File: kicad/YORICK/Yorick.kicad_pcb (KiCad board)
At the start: 2 copper layers, 124 x 112 mm, 64 parts, among them J1 Conn_01x12, J2 AVR-ISP-6, J3 AudioJack2_SwitchT, J4 USB_B_Micro, J5 AudioJack2_SwitchT, Q1 Q_NJFET_DSG, Q2 Q_NJFET_DSG, SW1 SW_Push, SW2 SW_Push, U1 4069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

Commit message: Changing value for opamp pulldown resistor
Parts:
- R22: value 100k -> 1m
- R37: value 39k -> 33k
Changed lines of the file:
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@@
         (effects (font (size 1 1) (thickness 0.15)))
     )
-    (fp_text value "39k" (at 6.858 0.508) (layer "F.Fab")
+    (fp_text value "33k" (at 6.858 0.508) (layer "F.Fab")
         (effects (font (size 1 1) (thickness 0.15)))
     )
@@
         (effects (font (size 1 1) (thickness 0.15)))
     )
-    (fp_text value "100k" (at 6.35 0.508 90) (layer "F.Fab")
-        (effects (font (size 1 1) (thickness 0.15)))
-    )
+    (fp_text value "1m" (at 6.35 0.508 90) (layer "F.Fab")
+        (effects (font (size 1 1) (thickness 0.15)))
+    )

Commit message: Tweaking values for some parts
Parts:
- R16, R25: value 47r -> 18r
- R20, R21: value 2k2 -> rled
- RV1, RV2, RV3: value 100k -> 100kB
- RV4: value 10k -> 10kB
- RV5: value 100k -> 100kA
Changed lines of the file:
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@@
     (descr "https://www.omron.com/ecb/products/pdf/en-b3f.pdf")
     (tags "tact sw push 6mm")
+    (property "Part" "Omron B3F-1070 Extended")
     (property "Sheetfile" "Yorick.kicad_sch")
     (property "Sheetname" "")
@@
         (effects (font (size 1 1) (thickness 0.15)))
     )
-    (fp_text value "47r" (at 6.858 0.508 90) (layer "F.Fab")
+    (fp_text value "18r" (at 6.858 0.508 90) (layer "F.Fab")
         (effects (font (size 1 1) (thickness 0.15)))
     )
@@
         (effects (font (size 1 1) (thickness 0.15)))
     )
-    (fp_text value "47r" (at 3.302 -0.508 90) (layer "F.Fab")
+    (fp_text value "18r" (at 3.302 -0.508 90) (layer "F.Fab")
         (effects (font (size 1 1) (thickness 0.15)))
     )
@@
         (effects (font (size 1 1) (thickness 0.15)))
     )
-    (fp_text value "2k2" (at 3.302 -0.508 90) (layer "F.Fab")
+    (fp_text value "rled" (at 3.302 -0.508 90) (layer "F.Fab")
         (effects (font (size 1 1) (thickness 0.15)))
     )
@@
         (effects (font (size 1 1) (thickness 0.15)))
     )
-    (fp_text value "100k" (at 2.032 -0.04 -180) (layer "F.Fab")
+    (fp_text value "100kB" (at 2.032 -0.04 -180) (layer "F.Fab")
         (effects (font (size 1 1) (thickness 0.15)))
     )
@@
         (effects (font (size 1 1) (thickness 0.15)))
     )
-    (fp_text value "100k" (at 1.778 -0.04 -180) (layer "F.Fab")
+    (fp_text value "100kB" (at 1.778 -0.04 -180) (layer "F.Fab")
         (effects (font (size 1 1) (thickness 0.15)))
     )
@@
         (effects (font (size 1 1) (thickness 0.15)))
     )
-    (fp_text value "10k" (at 1.912 -0.014) (layer "F.Fab")
+    (fp_text value "10kB" (at 1.912 -0.014) (layer "F.Fab")
         (effects (font (size 1 1) (thickness 0.15)))
     )
@@
         (effects (font (size 1 1) (thickness 0.15)))
     )
-    (fp_text value "100k" (at 2.166 -0.014) (layer "F.Fab")
+    (fp_text value "100kA" (at 2.166 -0.014) (layer "F.Fab")
         (effects (font (size 1 1) (thickness 0.15)))
     )
@@
         (effects (font (size 1 1) (thickness 0.15)))
     )
-    (fp_text value "2k2" (at 3.302 -0.508 90) (layer "F.Fab")
+    (fp_text value "rled" (at 3.302 -0.508 90) (layer "F.Fab")
         (effects (font (size 1 1) (thickness 0.15)))
     )
@@
         (effects (font (size 1 1) (thickness 0.15)))
     )
-    (fp_text value "100k" (at 1.912 -0.028) (layer "F.Fab")
+    (fp_text value "100kB" (at 1.912 -0.028) (layer "F.Fab")
         (effects (font (size 1 1) (thickness 0.15)))
     )

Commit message: Updating parts and build info
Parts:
- R20, R21: value rled -> 1k
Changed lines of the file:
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@@
         (effects (font (size 1 1) (thickness 0.15)))
     )
-    (fp_text value "rled" (at 3.302 -0.508 90) (layer "F.Fab")
+    (fp_text value "1k" (at 3.302 -0.508 90) (layer "F.Fab")
         (effects (font (size 1 1) (thickness 0.15)))
     )
@@
         (effects (font (size 1 1) (thickness 0.15)))
     )
-    (fp_text value "rled" (at 3.302 -0.508 90) (layer "F.Fab")
+    (fp_text value "1k" (at 3.302 -0.508 90) (layer "F.Fab")
         (effects (font (size 1 1) (thickness 0.15)))
     )

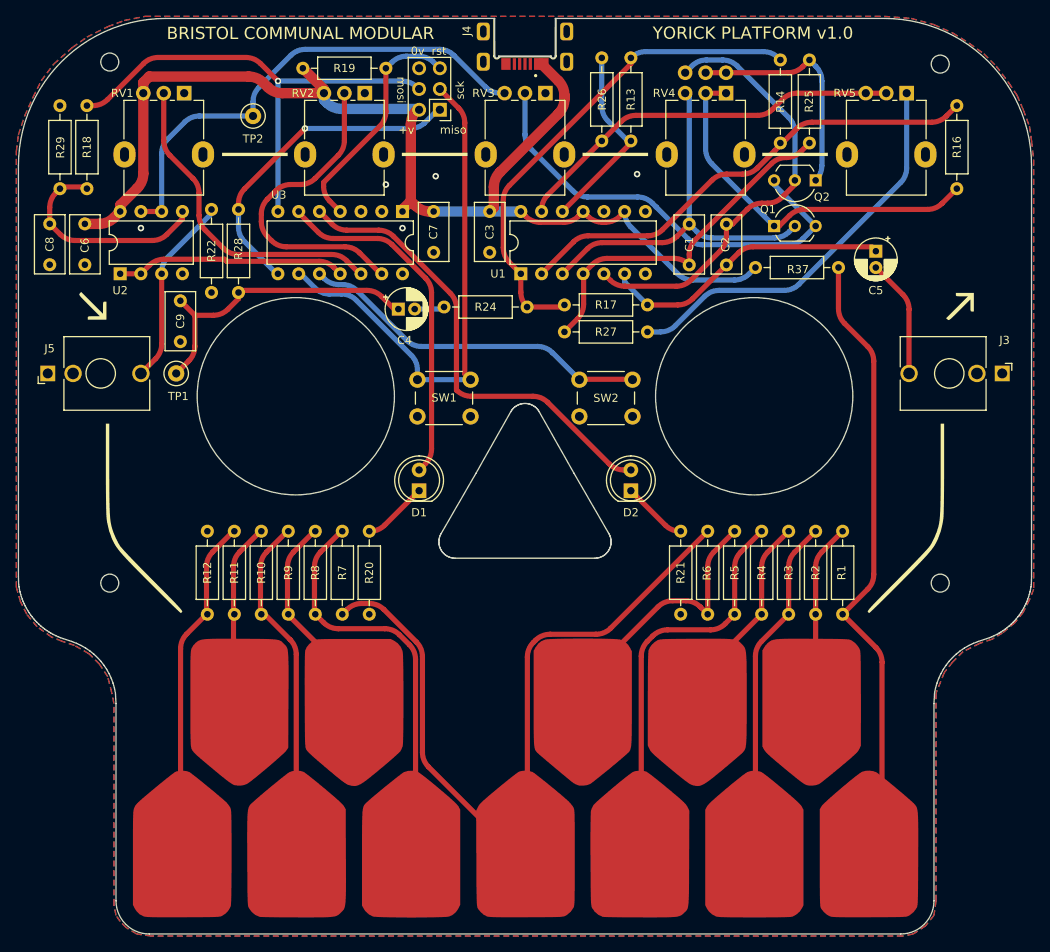
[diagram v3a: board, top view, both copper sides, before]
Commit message: Adding capacitors after some testing
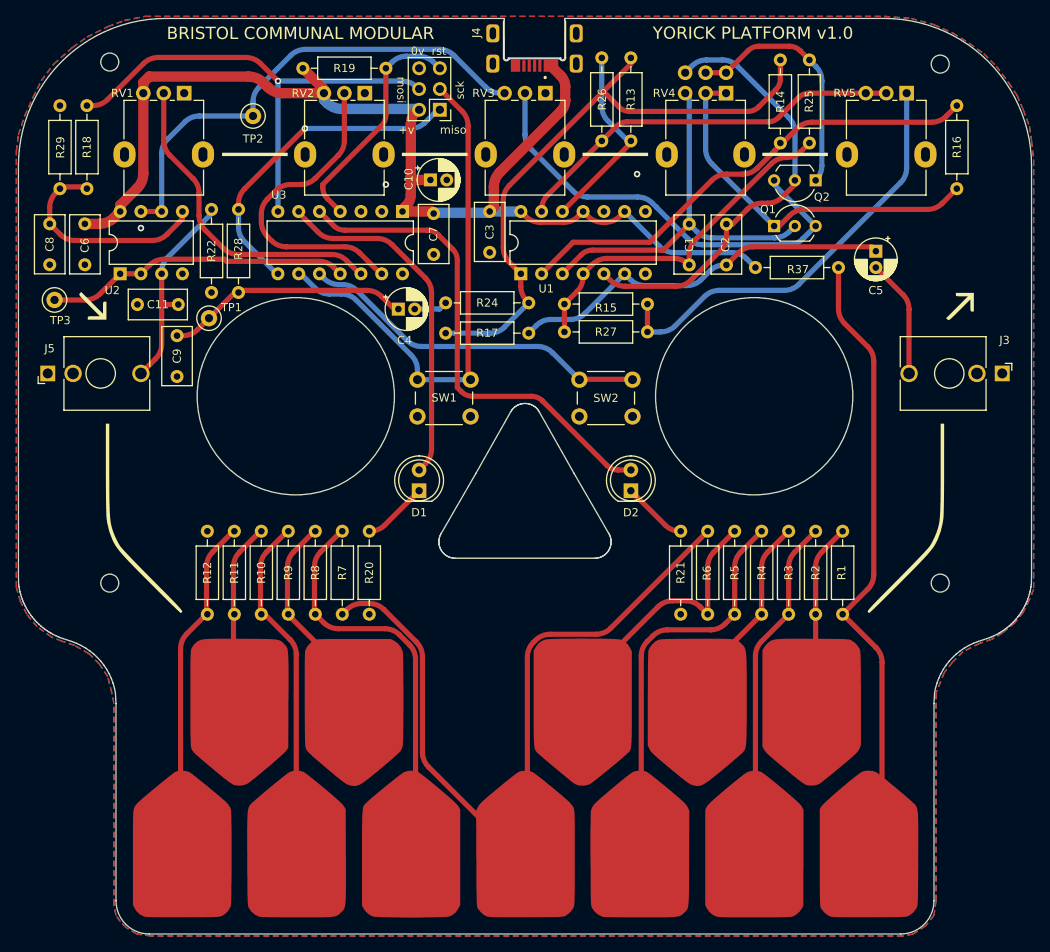
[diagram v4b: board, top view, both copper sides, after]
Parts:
- added C10: 10uF, Capacitor_THT:CP_Radial_D5.0mm_P2.00mm, F.Cu at (90.0, 55.3)
- added C11: 100pF, Capacitor_THT:C_Rect_L7.0mm_W3.5mm_P5.00mm, F.Cu at (54.2, 70.6)
- added R15: 10k, Resistor_THT:R_Axial_DIN0207_L6.3mm_D2.5mm_P10.16mm_Horizontal, F.Cu at (106.4, 70.5)
- added TP3: Freq In Test Point, TestPoint:TestPoint_Loop_D2.50mm_Drill1.0mm_LowProfile, F.Cu at (44.0, 70.0)
- R20, R21: value 1k -> 2k2
- R27: value 4k7 -> 10k
- moved R17 14.9 mm to (102.1, 74.1)
- moved TP1 7.86 mm to (62.9, 72.2)
- moved C9 4.29 mm to (59.0, 79.4)
- moved J4 1.19 mm to (102.8, 37.4)
- moved R24 0.55 mm to (102.1, 70.4)
- moved C7 0.25 mm to (90.4, 59.4)
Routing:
- net Net-(R13-Pad2): track 61.2 -> 75.7 mm
- net Net-(C2-Pad2): track 35.8 -> 47.5 mm
- net /MCU_ADC_1: track 28.2 -> 37.4 mm
- net Net-(C4-Pad1): track 37.4 -> 29.7 mm
- net Net-(R15-Pad2): track 49.3 -> 52.7 mm
- net /MCU_DOUT1: track 57.0 -> 60.2 mm
- net Net-(J5-T): track 23.4 -> 25.5 mm
- net Net-(Q2-D): track 28.7 -> 30.0 mm
- net VCC: track 146.3 -> 147.2 mm
- net Net-(C4-Pad2): track 3.33 -> 4.11 mm
- net GND: vias 5 -> 3
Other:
- outline, holes or cut-outs redrawn
